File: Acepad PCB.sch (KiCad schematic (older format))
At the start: 58 parts, among them SW1 SW_Push, U1 ATmega32U4-AU, Y1 16MHz

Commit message: Generated netlist and continued work on PCB
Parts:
- F1: footprint (none) -> Housings_QFP:TQFP-44_10x10mm_Pitch0.8mm
- MX1, MX10, MX12, MX13, MX14, MX15, MX16, MX17, MX18, MX19, MX2, MX20, MX3, MX4, MX5, MX6, MX7, MX8, MX9: footprint (none) -> MX_Alps_Hybrid:MX-1U
- MX11, MX21: footprint (none) -> MX_Alps_Hybrid:MX-2U
- R1, R2, R3, R4: footprint (none) -> Resistor_SMD:R_0805_2012Metric
- SW1: footprint (none) -> random-keyboard-parts:SKQG-1155865
- USB1: footprint (none) -> random-keyboard-parts:Molex-0548190589
- Y1: footprint (none) -> Crystal:Crystal_SMD_3225-4Pin_3.2x2.5mm
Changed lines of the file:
@@
 EESchema Schematic File Version 4
+LIBS:Acepad PCB-cache
 EELAYER 26 0
 EELAYER END
@@
 F 0 "R4" V 6479 4100 50  0000 C CNN
 F 1 "10k" V 6570 4100 50  0000 C CNN
-F 2 "" H 6675 4100 50  0001 C CNN
+F 2 "Resistor_SMD:R_0805_2012Metric" H 6675 4100 50  0001 C CNN
 F 3 "~" H 6675 4100 50  0001 C CNN
 	1    6675 4100
@@
 F 0 "R2" V 4504 3000 50  0000 C CNN
 F 1 "22" V 4595 3000 50  0000 C CNN
-F 2 "" H 4700 3000 50  0001 C CNN
+F 2 "Resistor_SMD:R_0805_2012Metric" H 4700 3000 50  0001 C CNN
 F 3 "~" H 4700 3000 50  0001 C CNN
 	1    4700 3000
@@
 F 0 "R1" V 4204 3100 50  0000 C CNN
 F 1 "22" V 4295 3100 50  0000 C CNN
-F 2 "" H 4400 3100 50  0001 C CNN
+F 2 "Resistor_SMD:R_0805_2012Metric" H 4400 3100 50  0001 C CNN
 F 3 "~" H 4400 3100 50  0001 C CNN
 	1    4400 3100
@@
 F 0 "Y1" V 4704 2466 50  0000 L CNN
 F 1 "16MHz" V 4795 2466 50  0000 L CNN
-F 2 "" H 4750 2300 50  0001 C CNN
+F 2 "Crystal:Crystal_SMD_3225-4Pin_3.2x2.5mm" H 4750 2300 50  0001 C CNN
 F 3 "~" H 4750 2300 50  0001 C CNN
 	1    4750 2300
@@
 F 0 "SW1" H 4900 2260 50  0000 C CNN
 F 1 "SW_Push" H 4900 2169 50  0000 C CNN
-F 2 "" H 4900 2175 50  0001 C CNN
+F 2 "random-keyboard-parts:SKQG-1155865" H 4900 2175 50  0001 C CNN
 F 3 "" H 4900 2175 50  0001 C CNN
 	1    4900 1975
@@
 F 0 "R3" H 5209 1721 50  0000 L CNN
 F 1 "10k" H 5209 1630 50  0000 L CNN
-F 2 "" H 5150 1675 50  0001 C CNN
+F 2 "Resistor_SMD:R_0805_2012Metric" H 5150 1675 50  0001 C CNN
 F 3 "~" H 5150 1675 50  0001 C CNN
 	1    5150 1675
@@
 F 0 "F1" V 2820 1825 50  0000 C CNN
 F 1 "500mA" V 2911 1825 50  0000 C CNN
-F 2 "" H 3075 1625 50  0001 L CNN
+F 2 "Housings_QFP:TQFP-44_10x10mm_Pitch0.8mm" H 3075 1625 50  0001 L CNN
 F 3 "~" H 3025 1825 50  0001 C CNN
 	1    3025 1825
@@
 F 0 "USB1" V 2612 1994 60  0000 C CNN
 F 1 "Molex-0548190589" V 2506 1994 60  0000 C CNN
-F 2 "" H 2075 2025 60  0001 C CNN
+F 2 "random-keyboard-parts:Molex-0548190589" H 2075 2025 60  0001 C CNN
 F 3 "" H 2075 2025 60  0001 C CNN
 	1    2075 2025
@@
 F 0 "MX6" H 8086 2017 60  0000 C CNN
 F 1 "MX-1U" H 8086 1943 20  0000 C CNN
-F 2 "" H 7975 1775 60  0001 C CNN
+F 2 "MX_Alps_Hybrid:MX-1U" H 7975 1775 60  0001 C CNN
 F 3 "" H 7975 1775 60  0001 C CNN
 	1    8000 1800
@@
 F 0 "MX8" H 8736 2017 60  0000 C CNN
 F 1 "MX-1U" H 8736 1943 20  0000 C CNN
-F 2 "" H 8625 1775 60  0001 C CNN
+F 2 "MX_Alps_Hybrid:MX-1U" H 8625 1775 60  0001 C CNN
 F 3 "" H 8625 1775 60  0001 C CNN
 	1    8650 1800
@@
 F 0 "MX15" H 9536 2017 60  0000 C CNN
 F 1 "MX-1U" H 9536 1943 20  0000 C CNN
-F 2 "" H 9425 1775 60  0001 C CNN
+F 2 "MX_Alps_Hybrid:MX-1U" H 9425 1775 60  0001 C CNN
 F 3 "" H 9425 1775 60  0001 C CNN
 	1    9450 1800
@@
 F 0 "MX1" H 7286 2017 60  0000 C CNN
 F 1 "MX-1U" H 7286 1943 20  0000 C CNN
-F 2 "" H 7175 1775 60  0001 C CNN
+F 2 "MX_Alps_Hybrid:MX-1U" H 7175 1775 60  0001 C CNN
 F 3 "" H 7175 1775 60  0001 C CNN
 	1    7200 1800
@@
 F 0 "MX3" H 7686 2017 60  0000 C CNN
 F 1 "MX-1U" H 7686 1943 20  0000 C CNN
-F 2 "" H 7575 1775 60  0001 C CNN
+F 2 "MX_Alps_Hybrid:MX-1U" H 7575 1775 60  0001 C CNN
 F 3 "" H 7575 1775 60  0001 C CNN
 	1    7600 1800
@@
 F 0 "MX2" H 7286 3742 60  0000 C CNN
 F 1 "MX-1U" H 7286 3668 20  0000 C CNN
-F 2 "" H 7175 3500 60  0001 C CNN
+F 2 "MX_Alps_Hybrid:MX-1U" H 7175 3500 60  0001 C CNN
 F 3 "" H 7175 3500 60  0001 C CNN
 	1    7200 3525
@@
 F 0 "MX5" H 7686 3742 60  0000 C CNN
 F 1 "MX-1U" H 7686 3668 20  0000 C CNN
-F 2 "" H 7575 3500 60  0001 C CNN
+F 2 "MX_Alps_Hybrid:MX-1U" H 7575 3500 60  0001 C CNN
 F 3 "" H 7575 3500 60  0001 C CNN
 	1    7600 3525
@@
 F 0 "MX4" H 7686 3167 60  0000 C CNN
 F 1 "MX-1U" H 7686 3093 20  0000 C CNN
-F 2 "" H 7575 2925 60  0001 C CNN
+F 2 "MX_Alps_Hybrid:MX-1U" H 7575 2925 60  0001 C CNN
 F 3 "" H 7575 2925 60  0001 C CNN
 	1    7600 2950
@@
 F 0 "MX7" H 8086 3742 60  0000 C CNN
 F 1 "MX-1U" H 8086 3668 20  0000 C CNN
-F 2 "" H 7975 3500 60  0001 C CNN
+F 2 "MX_Alps_Hybrid:MX-1U" H 7975 3500 60  0001 C CNN
 F 3 "" H 7975 3500 60  0001 C CNN
 	1    8000 3525
@@
 F 0 "MX12" H 9136 2017 60  0000 C CNN
 F 1 "MX-1U" H 9136 1943 20  0000 C CNN
-F 2 "" H 9025 1775 60  0001 C CNN
+F 2 "MX_Alps_Hybrid:MX-1U" H 9025 1775 60  0001 C CNN
 F 3 "" H 9025 1775 60  0001 C CNN
 	1    9050 1800
@@
 F 0 "MX9" H 8736 2592 60  0000 C CNN
 F 1 "MX-1U" H 8736 2518 20  0000 C CNN
-F 2 "" H 8625 2350 60  0001 C CNN
+F 2 "MX_Alps_Hybrid:MX-1U" H 8625 2350 60  0001 C CNN
 F 3 "" H 8625 2350 60  0001 C CNN
 	1    8650 2375
@@
 F 0 "MX13" H 9136 2592 60  0000 C CNN
 F 1 "MX-1U" H 9136 2518 20  0000 C CNN
-F 2 "" H 9025 2350 60  0001 C CNN
+F 2 "MX_Alps_Hybrid:MX-1U" H 9025 2350 60  0001 C CNN
 F 3 "" H 9025 2350 60  0001 C CNN
 	1    9050 2375
@@
 F 0 "MX16" H 9536 2592 60  0000 C CNN
 F 1 "MX-1U" H 9536 2518 20  0000 C CNN
-F 2 "" H 9425 2350 60  0001 C CNN
+F 2 "MX_Alps_Hybrid:MX-1U" H 9425 2350 60  0001 C CNN
 F 3 "" H 9425 2350 60  0001 C CNN
 	1    9450 2375
@@
 F 0 "MX10" H 8736 3167 60  0000 C CNN
 F 1 "MX-1U" H 8736 3093 20  0000 C CNN
-F 2 "" H 8625 2925 60  0001 C CNN
+F 2 "MX_Alps_Hybrid:MX-1U" H 8625 2925 60  0001 C CNN
 F 3 "" H 8625 2925 60  0001 C CNN
 	1    8650 2950
@@
 F 0 "MX14" H 9136 3167 60  0000 C CNN
 F 1 "MX-1U" H 9136 3093 20  0000 C CNN
-F 2 "" H 9025 2925 60  0001 C CNN
+F 2 "MX_Alps_Hybrid:MX-1U" H 9025 2925 60  0001 C CNN
 F 3 "" H 9025 2925 60  0001 C CNN
 	1    9050 2950
@@
 F 0 "MX17" H 9536 3167 60  0000 C CNN
 F 1 "MX-1U" H 9536 3093 20  0000 C CNN
-F 2 "" H 9425 2925 60  0001 C CNN
+F 2 "MX_Alps_Hybrid:MX-1U" H 9425 2925 60  0001 C CNN
 F 3 "" H 9425 2925 60  0001 C CNN
 	1    9450 2950
@@
 F 0 "MX18" H 9536 3742 60  0000 C CNN
 F 1 "MX-1U" H 9536 3668 20  0000 C CNN
-F 2 "" H 9425 3500 60  0001 C CNN
+F 2 "MX_Alps_Hybrid:MX-1U" H 9425 3500 60  0001 C CNN
 F 3 "" H 9425 3500 60  0001 C CNN
 	1    9450 3525
@@
 F 0 "MX20" H 9936 2592 60  0000 C CNN
 F 1 "MX-1U" H 9936 2518 20  0000 C CNN
-F 2 "" H 9825 2350 60  0001 C CNN
+F 2 "MX_Alps_Hybrid:MX-1U" H 9825 2350 60  0001 C CNN
 F 3 "" H 9825 2350 60  0001 C CNN
 	1    9850 2375
@@
 F 0 "MX19" H 9936 2017 60  0000 C CNN
 F 1 "MX-1U" H 9936 1943 20  0000 C CNN
-F 2 "" H 9825 1775 60  0001 C CNN
+F 2 "MX_Alps_Hybrid:MX-1U" H 9825 1775 60  0001 C CNN
 F 3 "" H 9825 1775 60  0001 C CNN
 	1    9850 1800
@@
 F 0 "MX11" H 8936 3742 60  0000 C CNN
 F 1 "MX-2U" H 8936 3668 20  0000 C CNN
-F 2 "" H 8825 3500 60  0001 C CNN
+F 2 "MX_Alps_Hybrid:MX-2U" H 8825 3500 60  0001 C CNN
 F 3 "" H 8825 3500 60  0001 C CNN
 	1    8850 3525
@@
 F 0 "MX21" H 9936 3417 60  0000 C CNN
 F 1 "MX-2U" H 9936 3343 20  0000 C CNN
-F 2 "" H 9825 3175 60  0001 C CNN
+F 2 "MX_Alps_Hybrid:MX-2U" H 9825 3175 60  0001 C CNN
 F 3 "" H 9825 3175 60  0001 C CNN
 	1    9850 3200

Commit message: worked more on PCB
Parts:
- removed D11: D_Small, Diode_SMD:D_SOD-123, symbol Device:D_Small
- added D33, D34, D36: D_Small, Diode_SMD:D_SOD-123, symbol Device:D_Small
- added MX261, MX331, MX34, MX36: MX-1U, MX_Alps_Hybrid:MX-1U, symbol MX_Alps_Hybrids:MX-1U
- added MX62: MX-2U, MX_Alps_Hybrid:MX-2U, symbol MX_Alps_Hybrids:MX-2U
- F1: footprint Housings_QFP:TQFP-44_10x10mm_Pitch0.8mm -> Fuse_Holders_and_Fuses:Fuse_SMD1206_Reflow
- renumbered D1 to D0, D3 to D1, D9 to D13, D13 to D14, D16 to D15, D20 to D16, D6 to D2, D4 to D21, D10 to D23, D14 to D24, D17 to D25, D21 to D26, D8 to D3, D2 to D30, D5 to D31, D7 to D32, D18 to D35, D12 to D4, D15 to D5, D19 to D6, MX1 to MX0, MX3 to MX1, MX9 to MX13, MX13 to MX14, MX16 to MX15, MX20 to MX16, MX6 to MX2, MX4 to MX21, MX10 to MX23, MX14 to MX24, MX17 to MX25, MX21 to MX262, MX8 to MX3, MX2 to MX30, MX5 to MX31, MX7 to MX32, MX11 to MX332, MX18 to MX35, MX12 to MX4, MX15 to MX5, MX19 to MX61
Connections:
- net COL0: now also U1.36 (PF7)
- net COL1: now also U1.27 (PD7)
- net COL2: now also U1.38 (PF5)
- net COL3: now also U1.39 (PF4), MX331.1 (COL)
- net COL4: now also U1.40 (PF1), MX34.1 (COL)
- net COL5: now also U1.1 (PE6)
- net COL6: now also U1.28 (PB4), MX261.1 (COL), MX36.1 (COL), MX62.1 (COL)
- net ROW0: now also U1.41 (PF0)
- net ROW1: now also U1.9 (PB1)
- net ROW2: now also U1.10 (PB2)
- net ROW3: now also U1.11 (PB3), D33.1 (K), D34.1 (K), D36.1 (K)
- net at MX21.2 (ROW): now also D21.2 (A)
- net at D6.2 (A), MX61.2 (ROW): now also MX62.2 (ROW)
- net at MX332.2 (ROW): now also D33.2 (A), MX331.2 (ROW)
- net at D26.2 (A), MX262.2 (ROW): now also MX261.2 (ROW)
- new net: D36.2 (A), MX36.2 (ROW)
- new net: D34.2 (A), MX34.2 (ROW)
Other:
- moved on the sheet: D26, D6

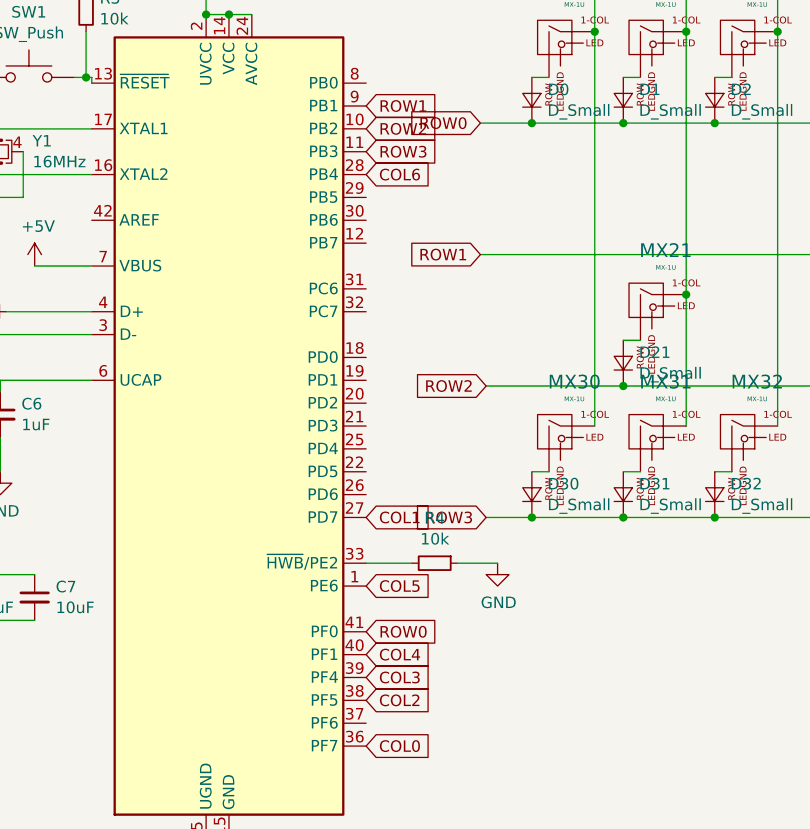
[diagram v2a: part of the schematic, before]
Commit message: continued work on pcb (flipped stabs, worked on wiring)
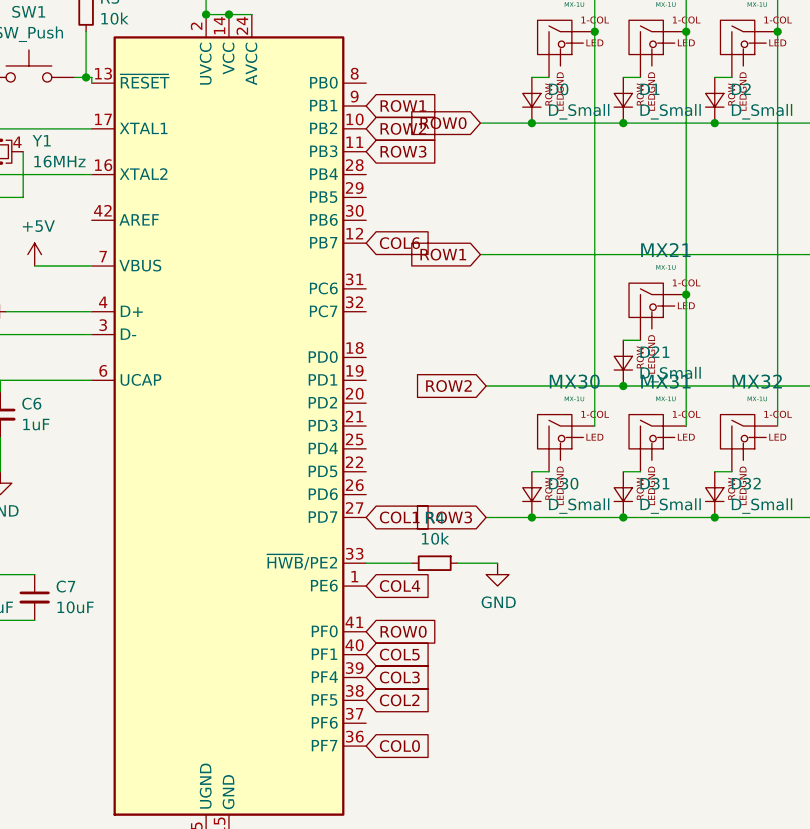
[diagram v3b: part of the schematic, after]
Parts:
- MX262, MX332, MX62: footprint MX_Alps_Hybrid:MX-2U -> MX_Alps_Hybrid:MX-2U-ReversedStabilizers
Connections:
- net COL4: now also U1.1 (PE6); no longer U1.40 (PF1)
- net COL5: now also U1.40 (PF1); no longer U1.1 (PE6)
- net COL6: now also U1.12 (PB7); no longer U1.28 (PB4)
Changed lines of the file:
@@
 F 0 "MX332" H 8936 3742 60  0000 C CNN
 F 1 "MX-2U" H 8936 3668 20  0000 C CNN
-F 2 "MX_Alps_Hybrid:MX-2U" H 8825 3500 60  0001 C CNN
+F 2 "MX_Alps_Hybrid:MX-2U-ReversedStabilizers" H 8825 3500 60  0001 C CNN
 F 3 "" H 8825 3500 60  0001 C CNN
 	1    8850 3525
@@
 F 0 "MX262" H 9936 3417 60  0000 C CNN
 F 1 "MX-2U" H 9936 3343 20  0000 C CNN
-F 2 "MX_Alps_Hybrid:MX-2U" H 9825 3175 60  0001 C CNN
+F 2 "MX_Alps_Hybrid:MX-2U-ReversedStabilizers" H 9825 3175 60  0001 C CNN
 F 3 "" H 9825 3175 60  0001 C CNN
 	1    9850 3200
@@
 F 0 "MX62" H 10286 2267 60  0000 C CNN
 F 1 "MX-2U" H 10286 2193 20  0000 C CNN
-F 2 "MX_Alps_Hybrid:MX-2U" H 10175 2025 60  0001 C CNN
+F 2 "MX_Alps_Hybrid:MX-2U-ReversedStabilizers" H 10175 2025 60  0001 C CNN
 F 3 "" H 10175 2025 60  0001 C CNN
 	1    10200 2050
@@
 Text GLabel 6375 4600 2    50   Input ~ 0
 COL3
+Text GLabel 6375 4200 2    50   Input ~ 0
+COL4
 Text GLabel 6375 4500 2    50   Input ~ 0
-COL4
-Text GLabel 6375 4200 2    50   Input ~ 0
 COL5
-Text GLabel 6375 2400 2    50   Input ~ 0
+Text GLabel 6375 2700 2    50   Input ~ 0
 COL6
 $EndSCHEMATC
